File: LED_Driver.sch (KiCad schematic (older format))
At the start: 0 parts

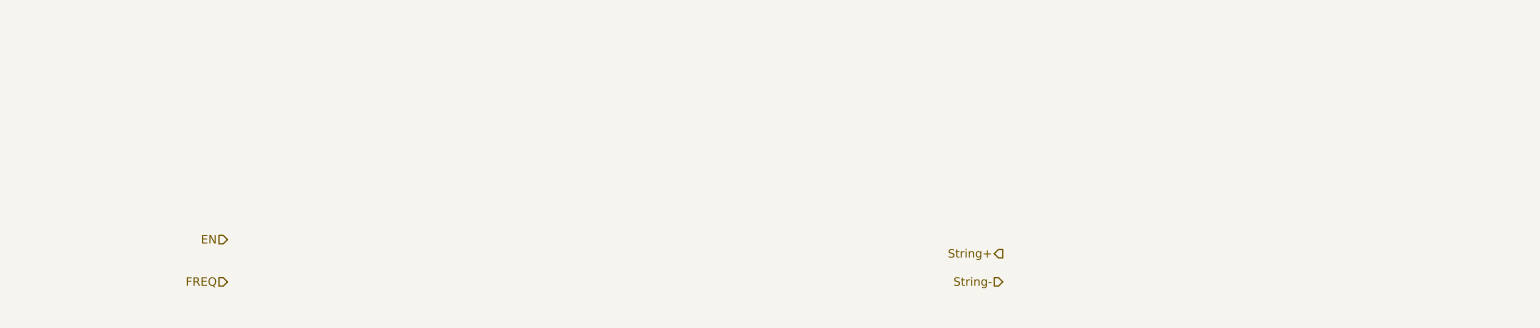
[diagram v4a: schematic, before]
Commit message: Create Arduino Schematic and Wire Up top Level
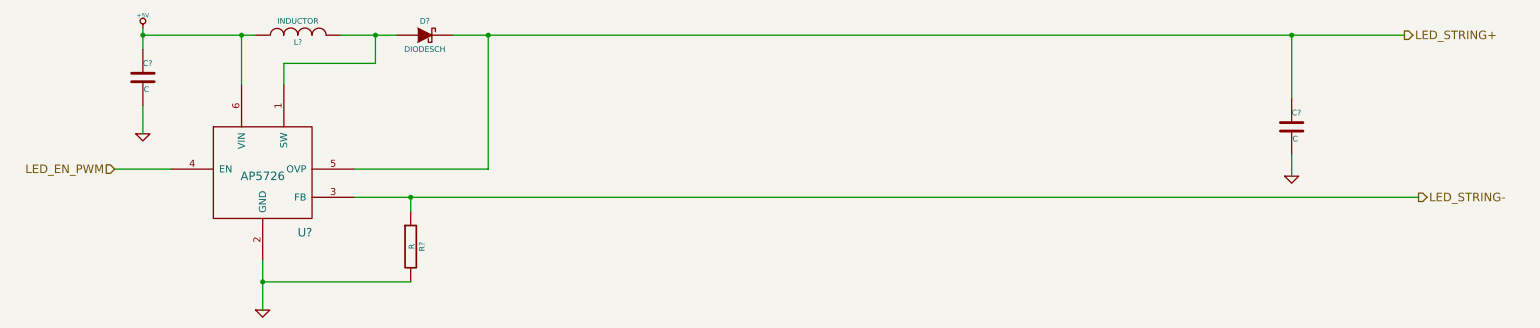
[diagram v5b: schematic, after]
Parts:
- added C? (x2): C, ~, symbol C
- added D?: DIODESCH, ~, symbol DIODESCH
- added L?: INDUCTOR, ~, symbol INDUCTOR
- added R?: R, ~, symbol R
- added U?: AP5726, symbol AP5726
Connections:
- new net: D?.1 (A), L?.2, U?.1 (SW)
- new net +5V: C?.1, L?.1, U?.6 (VIN)
- new net GND: C?.2, C?.2, R?.2, U?.2 (GND)
- new net LED_EN_PWM: U?.4 (EN)
- new net LED_STRING+: C?.1, D?.2 (K), U?.5 (OVP)
- new net LED_STRING-: R?.1, U?.3 (FB)
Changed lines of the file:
@@
 Comment4 ""
 $EndDescr
-Text HLabel 2000 2200 0    60   Input ~ 0
-EN
-Text HLabel 2000 2500 0    60   Input ~ 0
-FREQ
-Text HLabel 7500 2300 0    60   Output ~ 0
-String+
-Text HLabel 7500 2500 0    60   Input ~ 0
-String-
+Text HLabel 1200 1700 0    60   Input ~ 0
+LED_EN_PWM
+Text HLabel 10350 750  2    60   Output ~ 0
+LED_STRING+
+Text HLabel 10450 1900 2    60   Output ~ 0
+LED_STRING-
+$Comp
+L AP5726 U?
+U 1 1 52F2BE59
+P 2250 1800
+F 0 "U?" H 2550 1450 60  0000 C CNN
+F 1 "AP5726" H 2250 1850 60  0000 C CNN
+F 2 "" H 2250 1800 60  0000 C CNN
+F 3 "" H 2250 1800 60  0000 C CNN
+	1    2250 1800
+	1    0    0    -1
+$EndComp
+Wire Wire Line
+	1200 1700 1600 1700
+$Comp
+L +5V #PWR?
+U 1 1 52F2C07E
+P 1400 700
+F 0 "#PWR?" H 1400 790 20  0001 C CNN
+F 1 "+5V" H 1400 790 30  0000 C CNN
+F 2 "" H 1400 700 60  0000 C CNN
+F 3 "" H 1400 700 60  0000 C CNN
+	1    1400 700
+	1    0    0    -1
+$EndComp
+Wire Wire Line
+	2100 750  2100 1100
+$Comp
+L GND #PWR?
+U 1 1 52F2C099
+P 1400 1450
+F 0 "#PWR?" H 1400 1450 30  0001 C CNN
+F 1 "GND" H 1400 1380 30  0001 C CNN
+F 2 "" H 1400 1450 60  0000 C CNN
+F 3 "" H 1400 1450 60  0000 C CNN
+	1    1400 1450
+	1    0    0    -1
+$EndComp
+$Comp
+L C C?
+U 1 1 52F2C0A8
+P 1400 1050
+F 0 "C?" H 1400 1150 40  0000 L CNN
+F 1 "C" H 1406 965 40  0000 L CNN
+F 2 "~" H 1438 900 30  0000 C CNN
+F 3 "~" H 1400 1050 60  0000 C CNN
+	1    1400 1050
+	1    0    0    -1
+$EndComp
+Wire Wire Line
+	1400 1250 1400 1450
+Wire Wire Line
+	1400 700  1400 850
+Wire Wire Line
+	1400 750  2200 750
+Connection ~ 1400 750
+$Comp
+L INDUCTOR L?
+U 1 1 52F2C0D7
+P 2500 750
+F 0 "L?" V 2450 750 40  0000 C CNN
+F 1 "INDUCTOR" V 2600 750 40  0000 C CNN
+F 2 "~" H 2500 750 60  0000 C CNN
+F 3 "~" H 2500 750 60  0000 C CNN
+	1    2500 750
+	0    -1   -1   0
+$EndComp
+Connection ~ 2100 750
+Wire Wire Line
+	2400 1100 2400 950
+Wire Wire Line
+	2400 950  3050 950
+Wire Wire Line
+	3050 950  3050 750
+Wire Wire Line
+	2800 750  3200 750
+$Comp
+L DIODESCH D?
+U 1 1 52F2C0F9
+P 3400 750
+F 0 "D?" H 3400 850 40  0000 C CNN
+F 1 "DIODESCH" H 3400 650 40  0000 C CNN
+F 2 "~" H 3400 750 60  0000 C CNN
+F 3 "~" H 3400 750 60  0000 C CNN
+	1    3400 750
+	1    0    0    -1
+$EndComp
+Connection ~ 3050 750
+$Comp
+L C C?
+U 1 1 52F2C112
+P 9550 1400
+F 0 "C?" H 9550 1500 40  0000 L CNN
+F 1 "C" H 9556 1315 40  0000 L CNN
+F 2 "~" H 9588 1250 30  0000 C CNN
+F 3 "~" H 9550 1400 60  0000 C CNN
+	1    9550 1400
+	1    0    0    -1
+$EndComp
+Wire Wire Line
+	3600 750  10350 750
+Wire Wire Line
+	9550 750  9550 1200
+Connection ~ 9550 750
+$Comp
+L R R?
+U 1 1 52F2C159
+P 3300 2250
+F 0 "R?" V 3380 2250 40  0000 C CNN
+F 1 "R" V 3307 2251 40  0000 C CNN
+F 2 "~" V 3230 2250 30  0000 C CNN
+F 3 "~" H 3300 2250 30  0000 C CNN
+	1    3300 2250
+	1    0    0    -1
+$EndComp
+Wire Wire Line
+	3300 2500 2250 2500
+Wire Wire Line
+	2250 2350 2250 2700
+$Comp
+L GND #PWR?
+U 1 1 52F2C179
+P 2250 2700
+F 0 "#PWR?" H 2250 2700 30  0001 C CNN
+F 1 "GND" H 2250 2630 30  0001 C CNN
+F 2 "" H 2250 2700 60  0000 C CNN
+F 3 "" H 2250 2700 60  0000 C CNN
+	1    2250 2700
+	1    0    0    -1
+$EndComp
+Connection ~ 2250 2500
+Wire Wire Line
+	2900 1900 10450 1900
+Wire Wire Line
+	3300 1900 3300 2000
+Connection ~ 3300 1900
+Wire Wire Line
+	2900 1700 3850 1700
+Wire Wire Line
+	3850 1700 3850 750
+Connection ~ 3850 750
+$Comp
+L GND #PWR?
+U 1 1 52F2CFAE
+P 9550 1750
+F 0 "#PWR?" H 9550 1750 30  0001 C CNN
+F 1 "GND" H 9550 1680 30  0001 C CNN
+F 2 "" H 9550 1750 60  0000 C CNN
+F 3 "" H 9550 1750 60  0000 C CNN
+	1    9550 1750
+	1    0    0    -1
+$EndComp
+Wire Wire Line
+	9550 1600 9550 1750
 $EndSCHEMATC

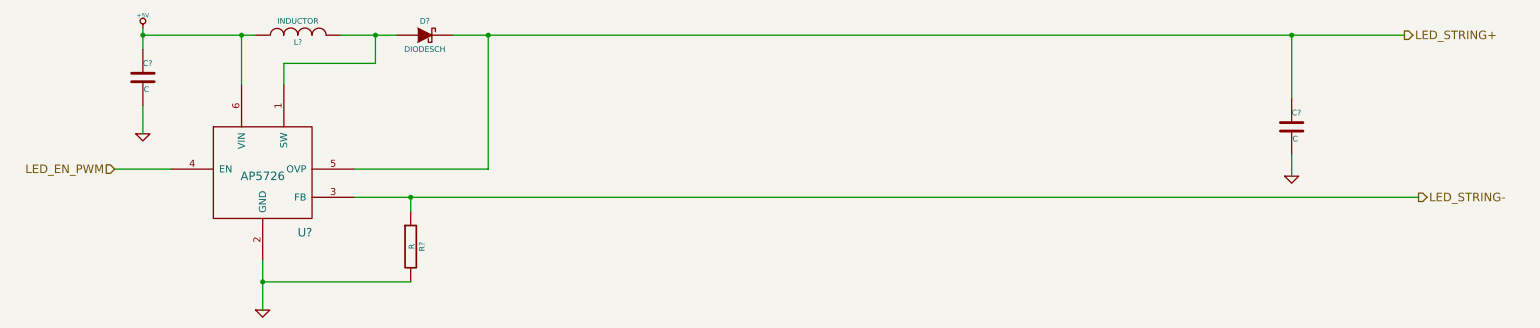
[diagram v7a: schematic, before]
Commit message: Added Arduino Connect Pin Layout
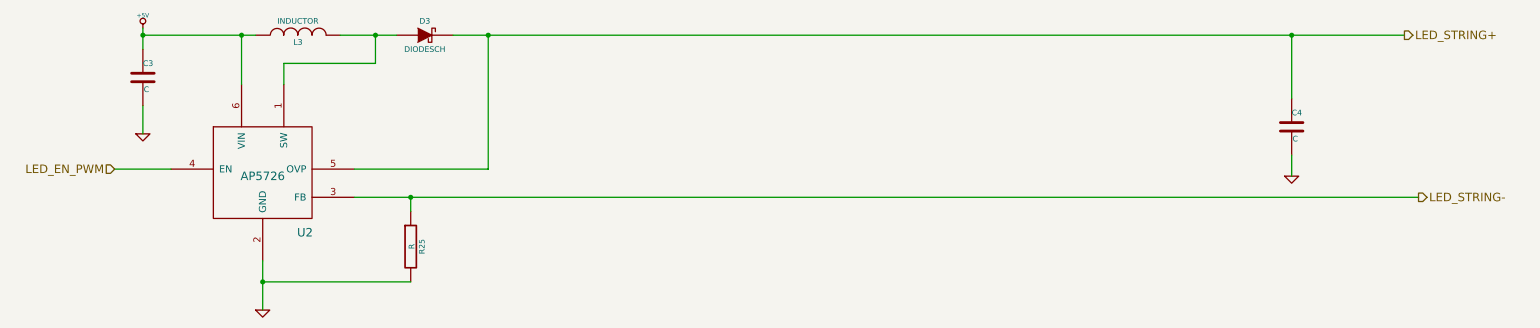
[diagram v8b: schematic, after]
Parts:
- gave numbers to parts that had none: 6
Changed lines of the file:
@@
 LED_STRING-
 $Comp
-L AP5726 U?
+L AP5726 U2
 U 1 1 52F2BE59
 P 2250 1800
-F 0 "U?" H 2550 1450 60  0000 C CNN
+F 0 "U2" H 2550 1450 60  0000 C CNN
 F 1 "AP5726" H 2250 1850 60  0000 C CNN
 F 2 "" H 2250 1800 60  0000 C CNN
@@
 	1200 1700 1600 1700
 $Comp
-L +5V #PWR?
+L +5V #PWR16
 U 1 1 52F2C07E
 P 1400 700
-F 0 "#PWR?" H 1400 790 20  0001 C CNN
+F 0 "#PWR16" H 1400 790 20  0001 C CNN
 F 1 "+5V" H 1400 790 30  0000 C CNN
 F 2 "" H 1400 700 60  0000 C CNN
@@
 	2100 750  2100 1100
 $Comp
-L GND #PWR?
+L GND #PWR17
 U 1 1 52F2C099
 P 1400 1450
-F 0 "#PWR?" H 1400 1450 30  0001 C CNN
+F 0 "#PWR17" H 1400 1450 30  0001 C CNN
 F 1 "GND" H 1400 1380 30  0001 C CNN
 F 2 "" H 1400 1450 60  0000 C CNN
@@
 $EndComp
 $Comp
-L C C?
+L C C3
 U 1 1 52F2C0A8
 P 1400 1050
-F 0 "C?" H 1400 1150 40  0000 L CNN
+F 0 "C3" H 1400 1150 40  0000 L CNN
 F 1 "C" H 1406 965 40  0000 L CNN
 F 2 "~" H 1438 900 30  0000 C CNN
@@
 Connection ~ 1400 750
 $Comp
-L INDUCTOR L?
+L INDUCTOR L3
 U 1 1 52F2C0D7
 P 2500 750
-F 0 "L?" V 2450 750 40  0000 C CNN
+F 0 "L3" V 2450 750 40  0000 C CNN
 F 1 "INDUCTOR" V 2600 750 40  0000 C CNN
 F 2 "~" H 2500 750 60  0000 C CNN
@@
 	2800 750  3200 750
 $Comp
-L DIODESCH D?
+L DIODESCH D3
 U 1 1 52F2C0F9
 P 3400 750
-F 0 "D?" H 3400 850 40  0000 C CNN
+F 0 "D3" H 3400 850 40  0000 C CNN
 F 1 "DIODESCH" H 3400 650 40  0000 C CNN
 F 2 "~" H 3400 750 60  0000 C CNN
@@
 Connection ~ 3050 750
 $Comp
-L C C?
+L C C4
 U 1 1 52F2C112
 P 9550 1400
-F 0 "C?" H 9550 1500 40  0000 L CNN
+F 0 "C4" H 9550 1500 40  0000 L CNN
 F 1 "C" H 9556 1315 40  0000 L CNN
 F 2 "~" H 9588 1250 30  0000 C CNN
@@
 Connection ~ 9550 750
 $Comp
-L R R?
+L R R25
 U 1 1 52F2C159
 P 3300 2250
-F 0 "R?" V 3380 2250 40  0000 C CNN
+F 0 "R25" V 3380 2250 40  0000 C CNN
 F 1 "R" V 3307 2251 40  0000 C CNN
 F 2 "~" V 3230 2250 30  0000 C CNN
@@
 	2250 2350 2250 2700
 $Comp
-L GND #PWR?
+L GND #PWR18
 U 1 1 52F2C179
 P 2250 2700
-F 0 "#PWR?" H 2250 2700 30  0001 C CNN
+F 0 "#PWR18" H 2250 2700 30  0001 C CNN
 F 1 "GND" H 2250 2630 30  0001 C CNN
 F 2 "" H 2250 2700 60  0000 C CNN
@@
 Connection ~ 3850 750
 $Comp
-L GND #PWR?
+L GND #PWR19
 U 1 1 52F2CFAE
 P 9550 1750
-F 0 "#PWR?" H 9550 1750 30  0001 C CNN
+F 0 "#PWR19" H 9550 1750 30  0001 C CNN
 F 1 "GND" H 9550 1680 30  0001 C CNN
 F 2 "" H 9550 1750 60  0000 C CNN
